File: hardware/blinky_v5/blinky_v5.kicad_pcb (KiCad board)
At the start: 2 copper layers, 130 x 70 mm, 241 parts, among them J1 RJ45, J12 Conn_01x06, J2 Conn_01x06_Pin, J3 Conn_01x05_Pin, J4 Conn_01x04_Pin, J5 Conn_01x06_Pin, J6 Conn_01x04_Pin, J7 Conn_01x04_Pin, J8 Conn_01x02, J9 Conn_02x10_Odd_Even, Q1 2N7002, Q10 2N7002, Q2 2N7002, Q3 2N7002, Q4 2N7002, Q5 2N7002, Q6 2N7002, Q7 2N7002, Q8 2N7002, Q9 2N7002, U1 ADA4807-1, U10 STM32F405RGTx, U11 AMS1117-3.3, U12 BA50DD0WHFP-TR, U13 M24C02-RMN, U2 SN74LVC1G14DBV, U3 SN74LVC1G14DBV, U4 ADA4807-1, U5 ADA4807-1, U6 TLV3603DCKR, U7 SN74LVC1G14DBV, U8 TLV3603DCKR, U9 L78L05_SOT89, X2 GTXO-14V (2.048MHz), Y1 AOCJY4A-10.000MHZ-SW, Y2 16MHz

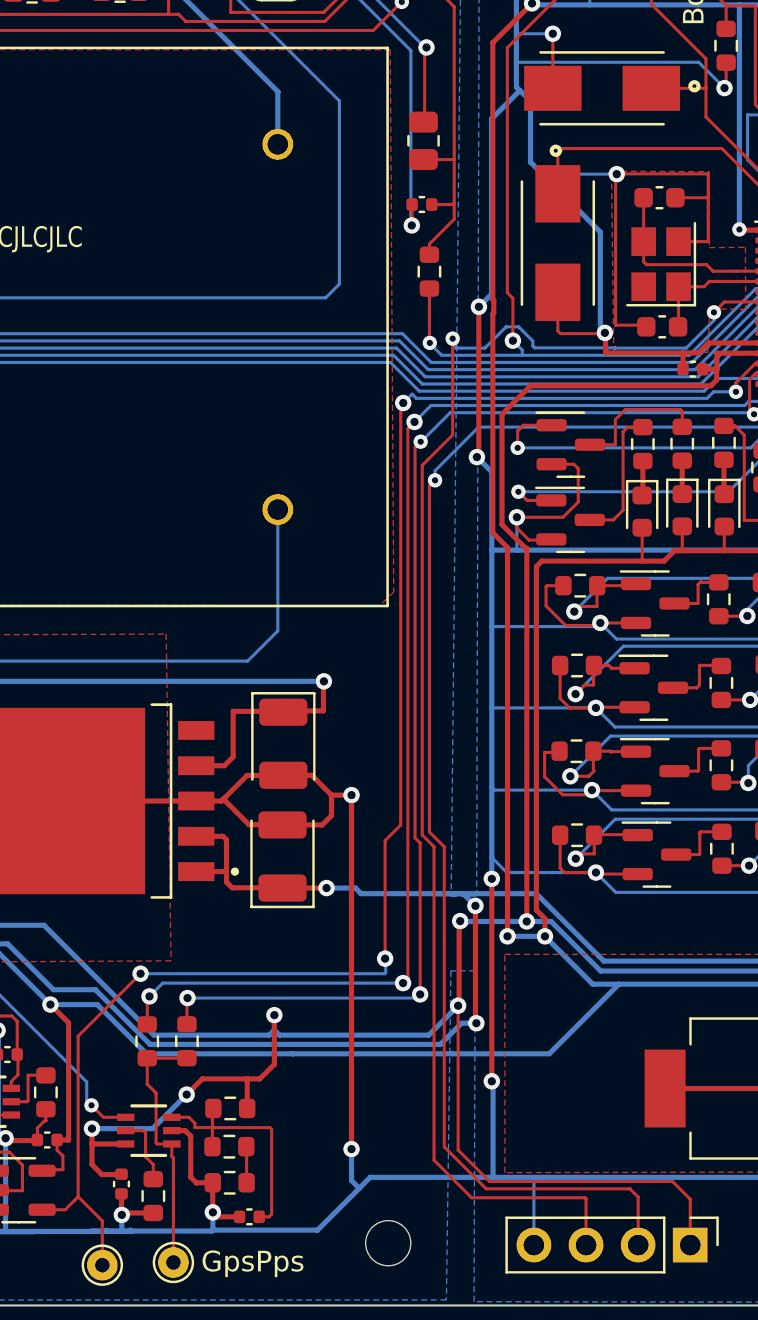
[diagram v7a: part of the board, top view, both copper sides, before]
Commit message: change color of status LEDs
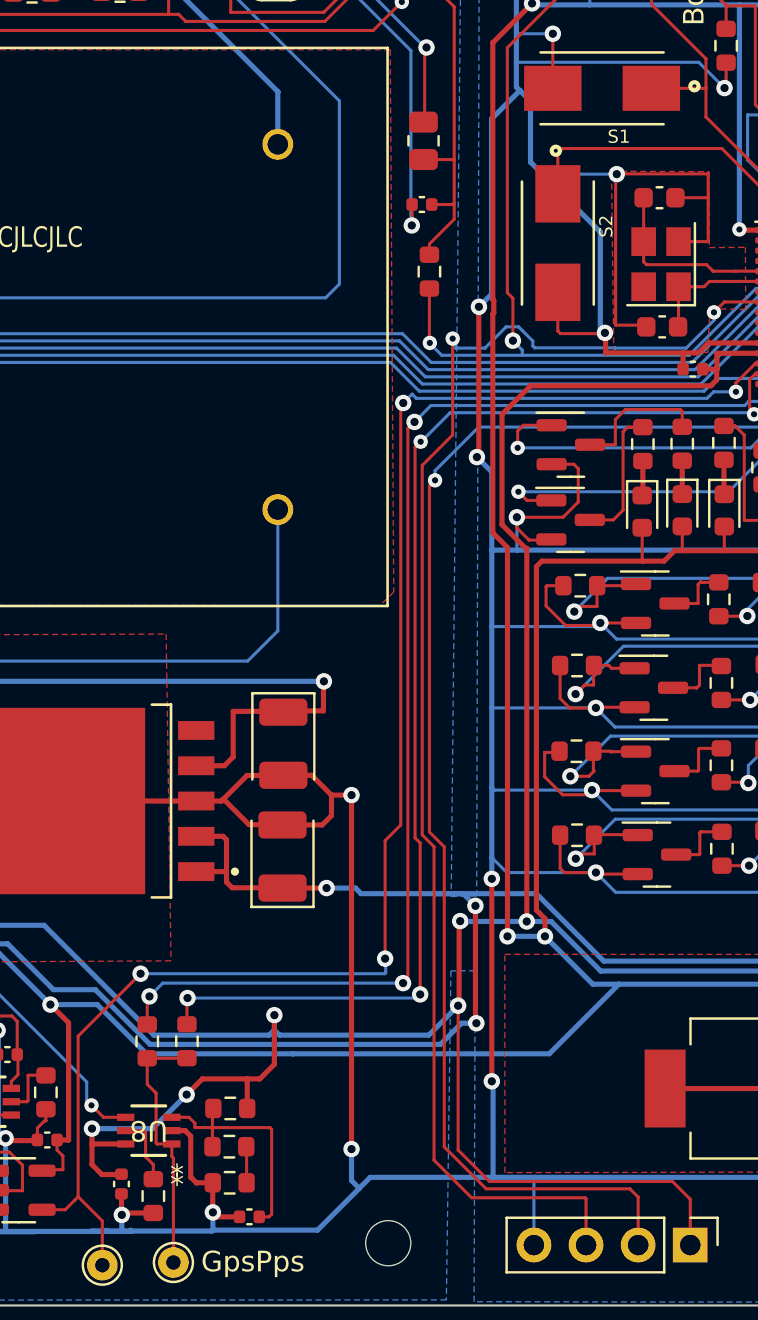
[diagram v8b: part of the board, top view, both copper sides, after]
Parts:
- D2: value LED-RED -> LED-G
- D3: value LED-RED -> LED-Y
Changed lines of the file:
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@@
     (descr "LED SMD 0603 (1608 Metric), square (rectangular) end terminal, IPC_7351 nominal, (Body size source: http://www.tortai-tech.com/upload/download/2011102023233369053.pdf), generated with kicad-footprint-generator")
     (tags "LED")
-    (property "LCSC" "C94869")
+    (property "LCSC" "C125093")
     (property "Sheetfile" "blinky_v5.kicad_sch")
     (property "Sheetname" "")
@@
         (effects (font (size 1 1) (thickness 0.15)))
     )
-    (fp_text value "LED-RED" (at 0 1.43 -90) (layer "F.Fab")
+    (fp_text value "LED-G" (at 0 1.43 -90) (layer "F.Fab")
         (effects (font (size 1 1) (thickness 0.15)))
     )
@@
     (property "Sheetname" "")
     (attr smd)
-    (fp_text reference "S1" (at -0.818505 -2.357851 180) (layer "F.SilkS") hide
+    (fp_text reference "S1" (at -0.818505 -2.357851 180) (layer "F.SilkS")
         (effects (font (size 0.640395 0.640395) (thickness 0.15)))
     )
@@
     (property "Sheetname" "")
     (attr smd)
-    (fp_text reference "S2" (at -0.818505 -2.357851 -90) (layer "F.SilkS") hide
+    (fp_text reference "S2" (at -0.818505 -2.357851 -90) (layer "F.SilkS")
         (effects (font (size 0.640395 0.640395) (thickness 0.15)))
     )
@@
     (descr "LED SMD 0603 (1608 Metric), square (rectangular) end terminal, IPC_7351 nominal, (Body size source: http://www.tortai-tech.com/upload/download/2011102023233369053.pdf), generated with kicad-footprint-generator")
     (tags "LED")
-    (property "LCSC" "C94869")
+    (property "LCSC" "C72038")
     (property "Sheetfile" "blinky_v5.kicad_sch")
     (property "Sheetname" "")
@@
         (effects (font (size 1 1) (thickness 0.15)))
     )
-    (fp_text value "LED-RED" (at 0 1.43 -90) (layer "F.Fab")
+    (fp_text value "LED-Y" (at 0 1.43 -90) (layer "F.Fab")
         (effects (font (size 1 1) (thickness 0.15)))
     )
@@
     (property "ki_keywords" "TLV3603DCKR")
     (attr smd)
-    (fp_text reference "U8" (at 0 0 180 unlocked) (layer "F.SilkS") hide
+    (fp_text reference "U8" (at 0 0 180 unlocked) (layer "F.SilkS")
         (effects (font (size 1 1) (thickness 0.15)))
     )
@@
         (effects (font (size 1 1) (thickness 0.15)))
     )
-    (fp_text user "*" (at -0.3175 -1.0033 180) (layer "F.Fab")
+    (fp_text user "*" (at -1.37795 -2.1486 180) (layer "F.SilkS")
+        (effects (font (size 1 1) (thickness 0.15)))
+    )
+    (fp_text user "*" (at -1.37795 -2.1486 180 unlocked) (layer "F.SilkS")
         (effects (font (size 1 1) (thickness 0.15)))
     )
@@
         (effects (font (size 1 1) (thickness 0.15)))
     )
+    (fp_text user "*" (at -0.3175 -1.0033 180) (layer "F.Fab")
+        (effects (font (size 1 1) (thickness 0.15)))
+    )
